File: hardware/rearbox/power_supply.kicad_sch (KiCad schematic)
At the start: 37 parts, among them U3 LM62440-Q1, U4 TLV743P

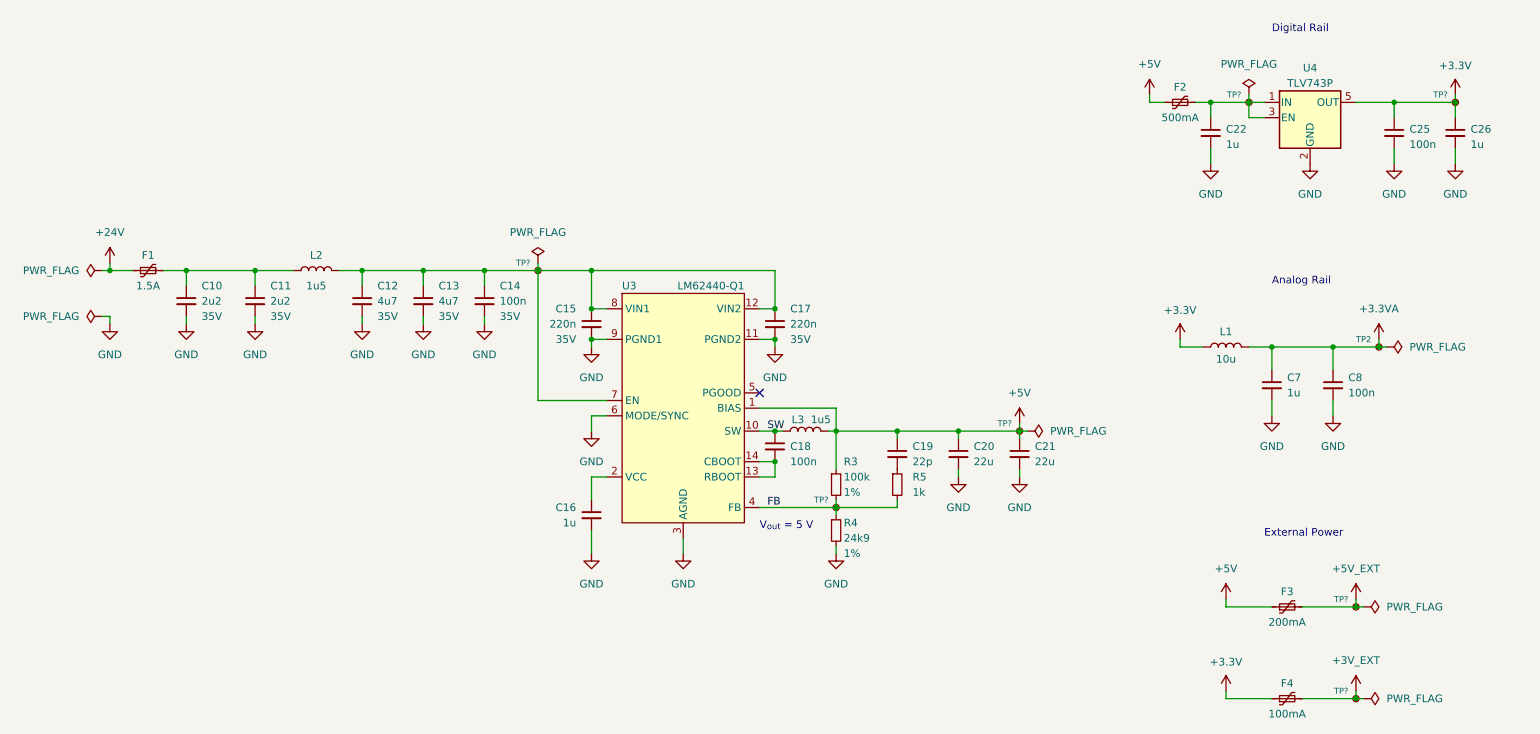
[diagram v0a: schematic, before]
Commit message: Place components on the PCB
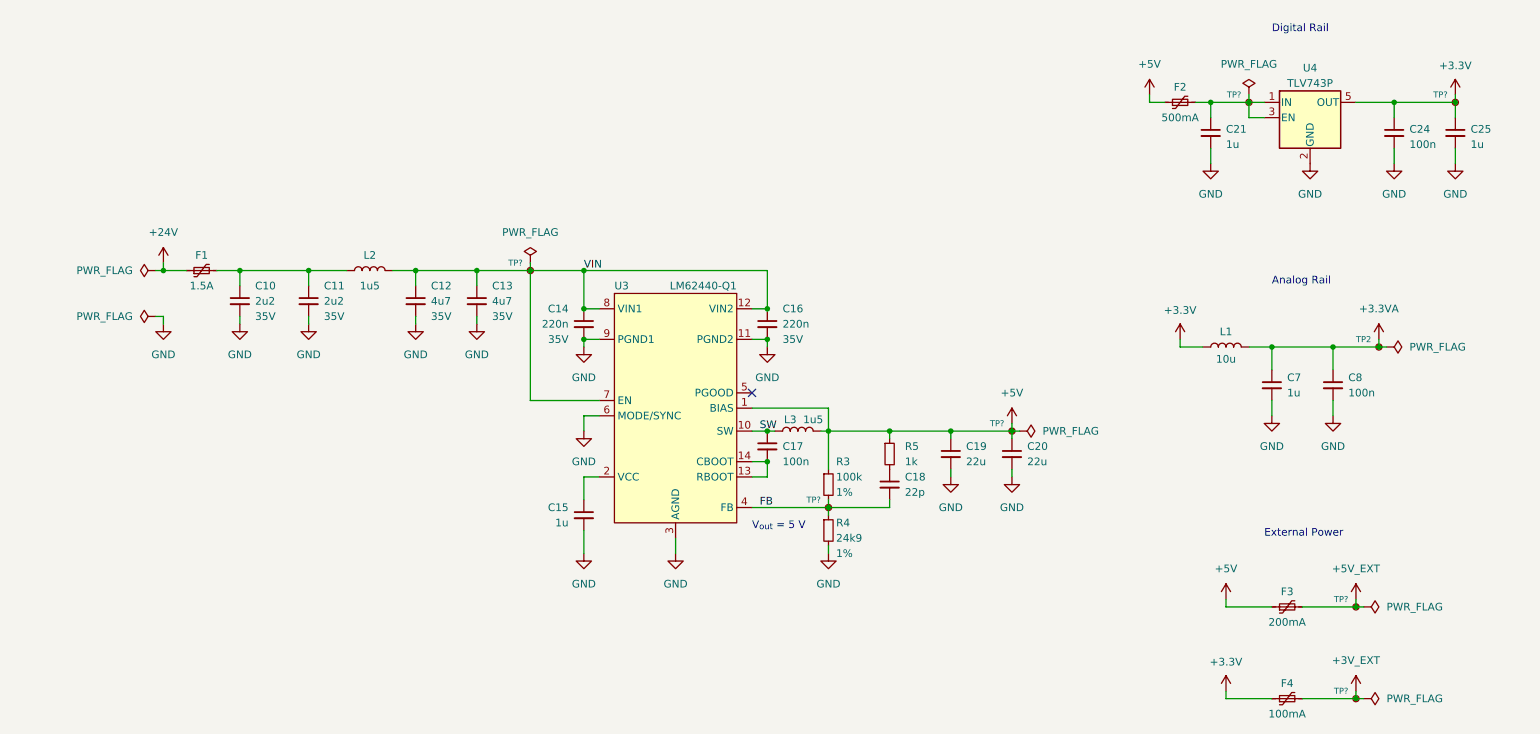
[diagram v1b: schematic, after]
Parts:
- removed C14: 100n, Capacitor_SMD:C_0603_1608Metric, symbol Device:C_Small
- C10, C11, C12, C13: footprint Capacitor_SMD:C_0603_1608Metric -> Capacitor_SMD:C_0805_2012Metric
- C14: renamed from C15; footprint Capacitor_SMD:C_0603_1608Metric -> Capacitor_SMD:C_0805_2012Metric
- C16: renamed from C17; footprint Capacitor_SMD:C_0603_1608Metric -> Capacitor_SMD:C_0805_2012Metric
- renumbered C16 to C15, C18 to C17, C19 to C18, C20 to C19, C21 to C20, C22 to C21, C25 to C24, C26 to C25
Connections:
- net +5V: now also R5.1; no longer C18.1
- net FB: now also C18.2; no longer R5.2
- net VIN: now reaches C12.1, C13.1, C14.1, C16.1, L2.2, TP?.1, U3.12 (VIN2), U3.7 (EN), U3.8 (VIN1)
- new net: C18.1, R5.2
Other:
- moved on the sheet: C10, C11, C12, C13, C14, C15, C16, C17, C18, C19, C20, F1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

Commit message: Align footprint references
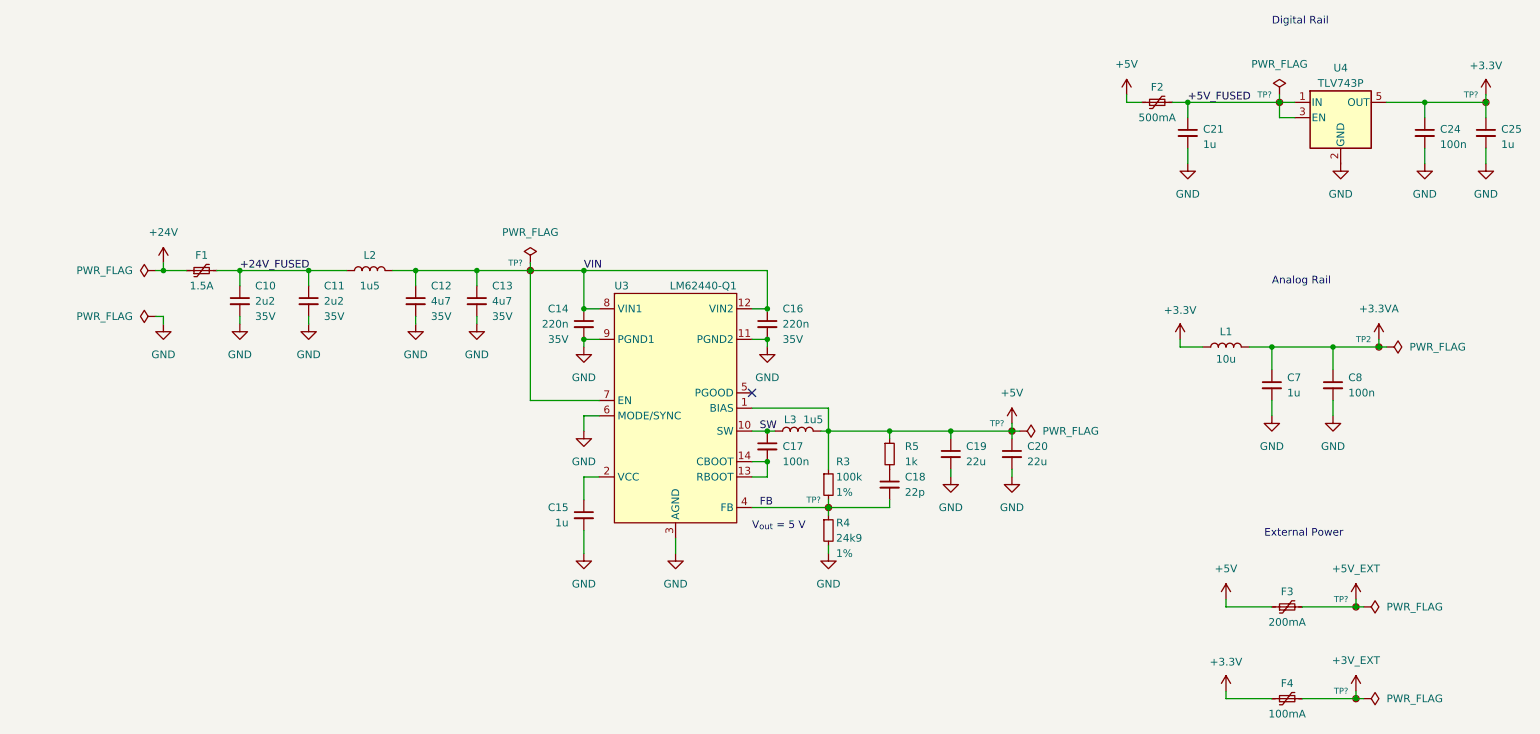
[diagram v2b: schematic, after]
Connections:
- net +5V_FUSED: now reaches C21.1, F2.2, TP?.1, U4.1 (IN), U4.3 (EN)
- net +24V_FUSED: now reaches C10.1, C11.1, F1.2, L2.1
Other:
- moved on the sheet: C21, C24, C25, F2, TP?, U4

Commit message: Route PCB tracks
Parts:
- F1, F2, F3, F4: footprint Fuse:Fuse_1812_4532Metric -> Local_Library:Fuse_1812_4532Metric
- L2, L3: footprint Inductor_SMD:L_Abracon_ASPI-4030S -> Local_Library:L_Abracon_ASPI-4030S
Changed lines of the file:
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@@
       (effects (font (size 1.27 1.27)))
     )
-    (property "Footprint" "Fuse:Fuse_1812_4532Metric" (at 240.03 144.78 0)
+    (property "Footprint" "Local_Library:Fuse_1812_4532Metric" (at 240.03 144.78 0)
       (effects (font (size 1.27 1.27)) (justify left) hide)
     )
@@
       (effects (font (size 1.27 1.27)))
     )
-    (property "Footprint" "Inductor_SMD:L_Abracon_ASPI-4030S" (at 82.55 74.93 0)
+    (property "Footprint" "Local_Library:L_Abracon_ASPI-4030S" (at 82.55 74.93 0)
       (effects (font (size 1.27 1.27)) hide)
     )
@@
       (effects (font (size 1.27 1.27)))
     )
-    (property "Footprint" "Inductor_SMD:L_Abracon_ASPI-4030S" (at 153.67 101.6 0)
+    (property "Footprint" "Local_Library:L_Abracon_ASPI-4030S" (at 153.67 101.6 0)
       (effects (font (size 1.27 1.27)) hide)
     )
@@
       (effects (font (size 1.27 1.27)))
     )
-    (property "Footprint" "Fuse:Fuse_1812_4532Metric" (at 59.69 73.66 0)
+    (property "Footprint" "Local_Library:Fuse_1812_4532Metric" (at 59.69 73.66 0)
       (effects (font (size 1.27 1.27)) (justify left) hide)
     )
@@
       (effects (font (size 1.27 1.27)))
     )
-    (property "Footprint" "Fuse:Fuse_1812_4532Metric" (at 240.03 129.54 0)
+    (property "Footprint" "Local_Library:Fuse_1812_4532Metric" (at 240.03 129.54 0)
       (effects (font (size 1.27 1.27)) (justify left) hide)
     )
@@
       (effects (font (size 1.27 1.27)))
     )
-    (property "Footprint" "Fuse:Fuse_1812_4532Metric" (at 218.44 45.72 0)
+    (property "Footprint" "Local_Library:Fuse_1812_4532Metric" (at 218.44 45.72 0)
       (effects (font (size 1.27 1.27)) (justify left) hide)
     )

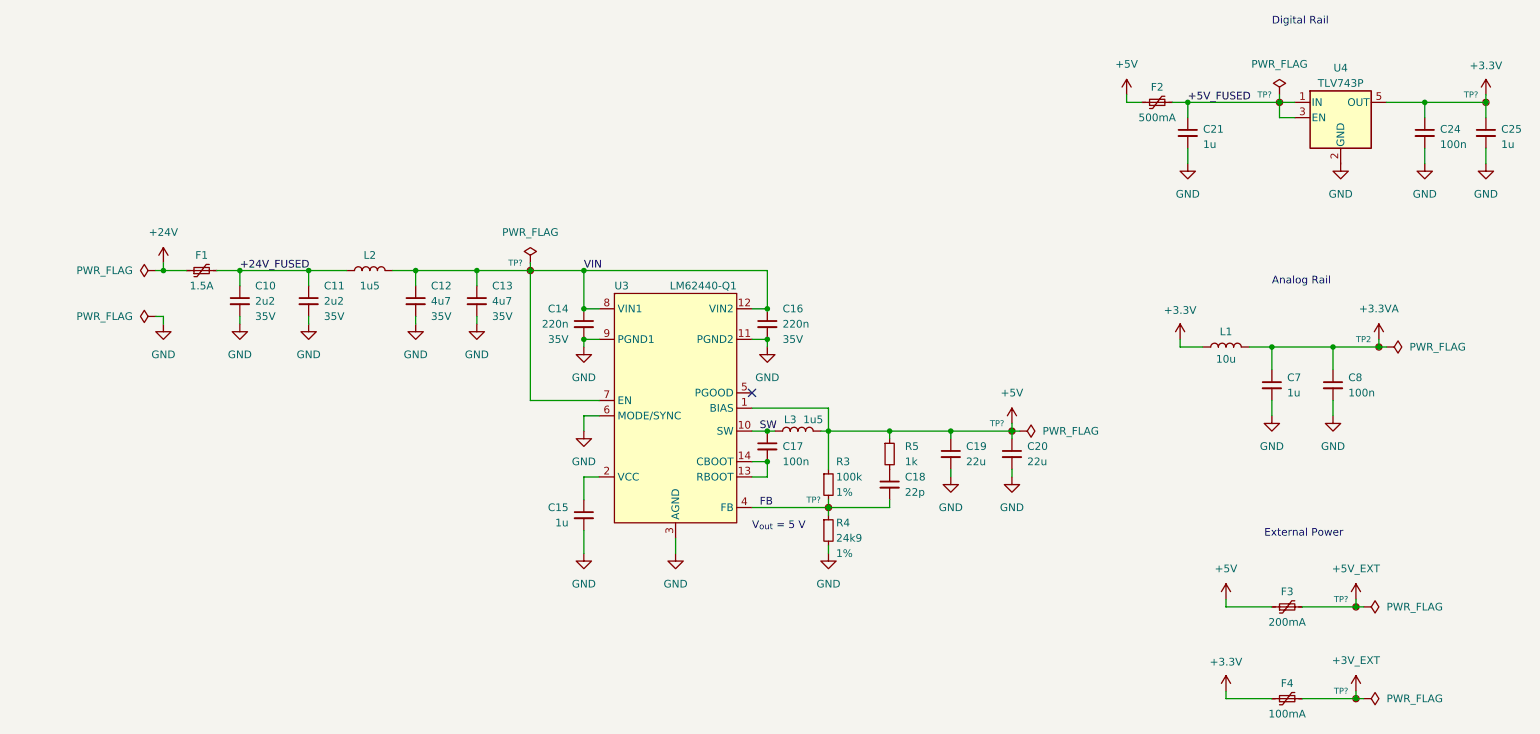
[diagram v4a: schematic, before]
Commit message: Route the tracks on the connector PCB
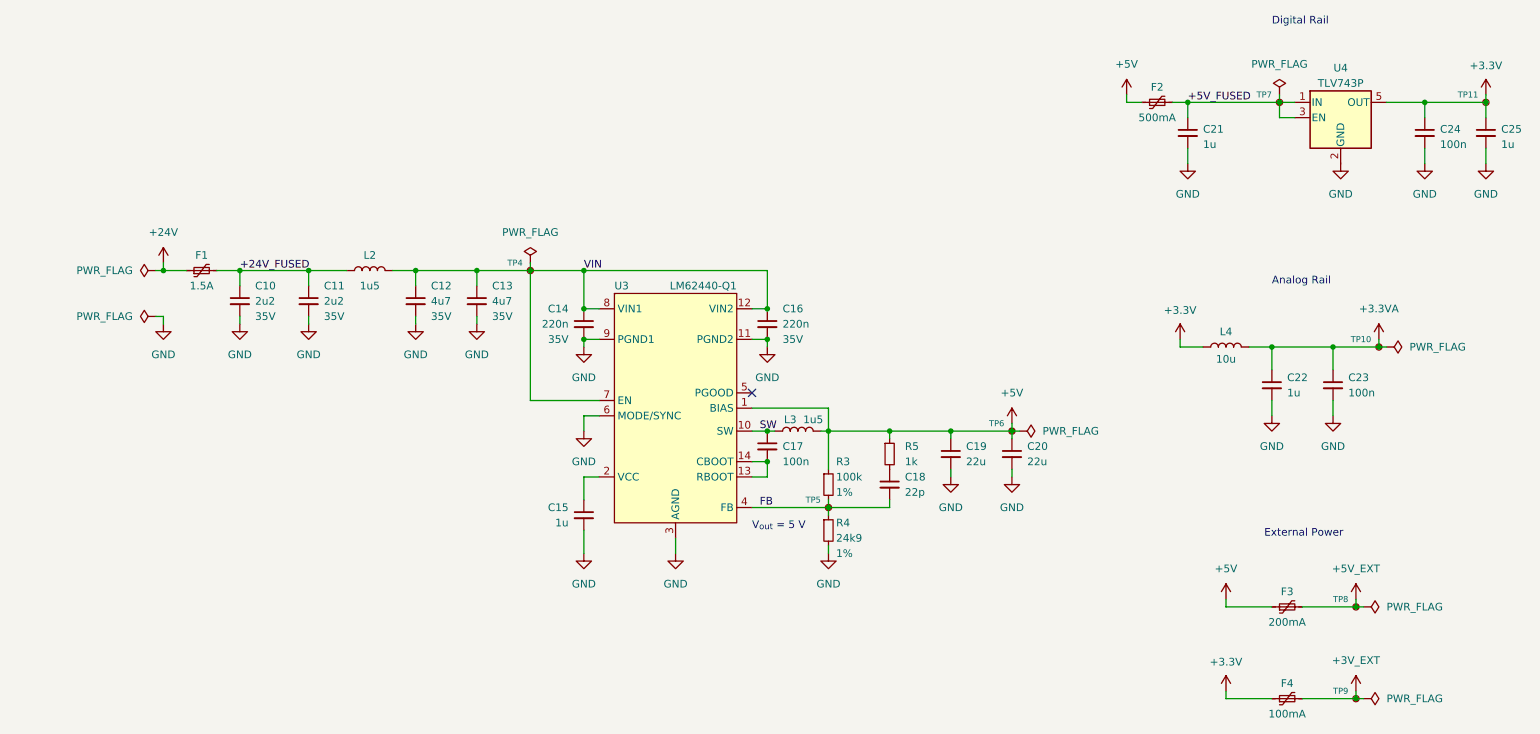
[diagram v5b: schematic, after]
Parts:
- gave numbers to parts that had none: 7
- renumbered C7 to C22, C8 to C23, L1 to L4, TP2 to TP10

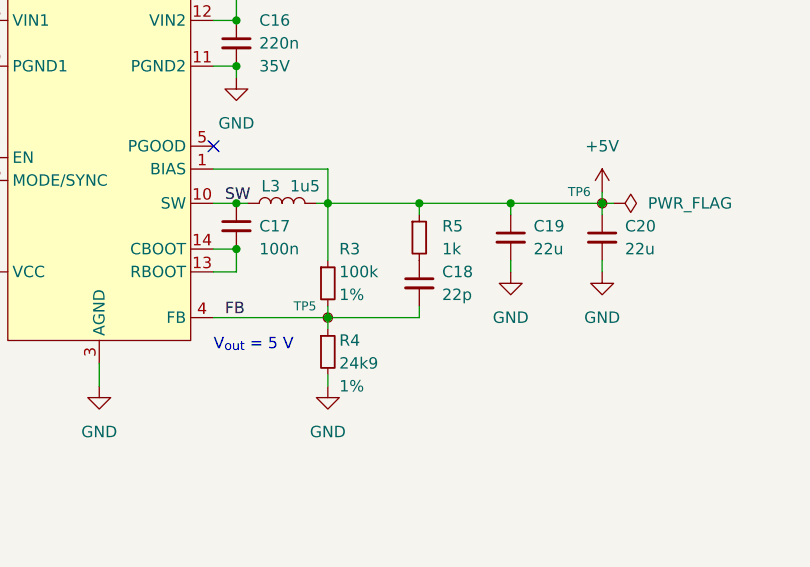
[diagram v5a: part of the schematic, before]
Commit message: Fix measurement bridges polarity
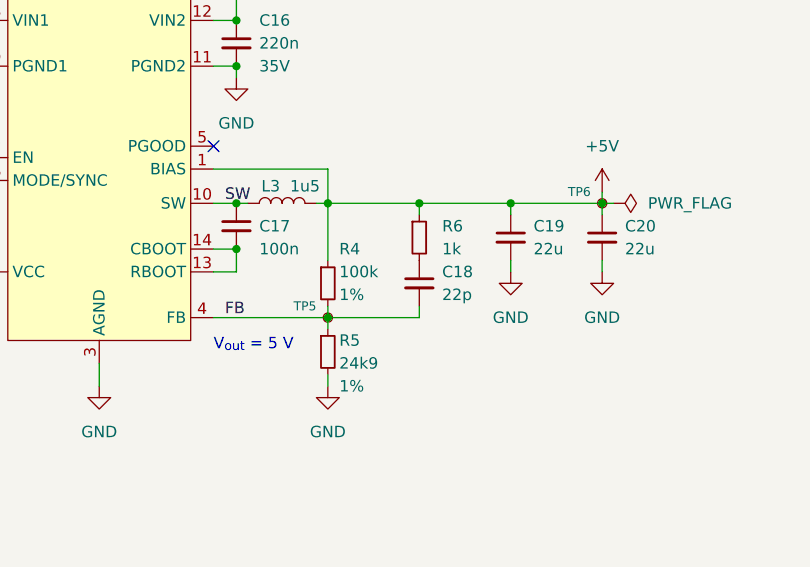
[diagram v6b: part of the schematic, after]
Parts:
- renumbered R3 to R4, R4 to R5, R5 to R6

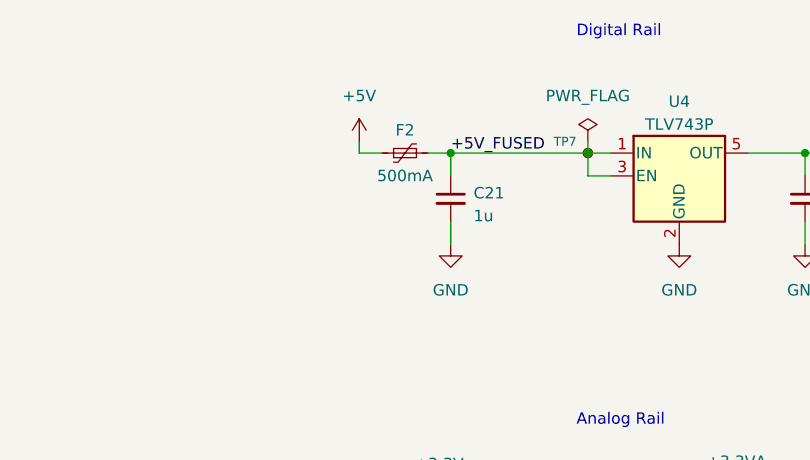
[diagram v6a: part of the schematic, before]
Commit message: Update schematic to reflect hardware changes
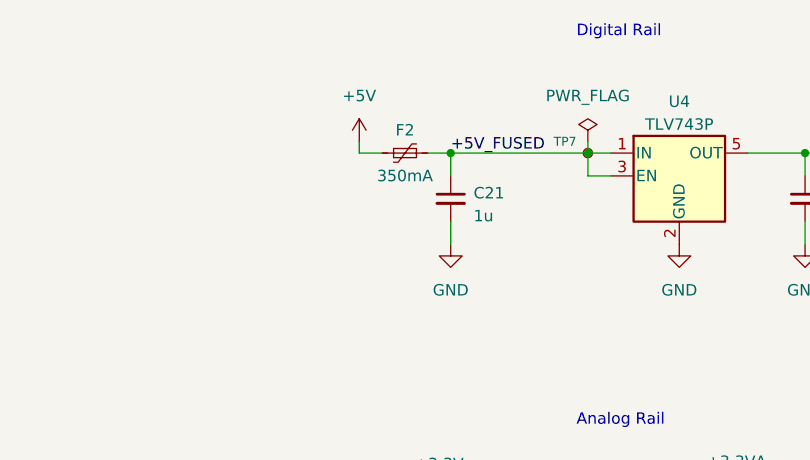
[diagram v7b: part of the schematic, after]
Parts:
- F2: value 500mA -> 350mA
